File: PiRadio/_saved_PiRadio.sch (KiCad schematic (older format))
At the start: 2 parts

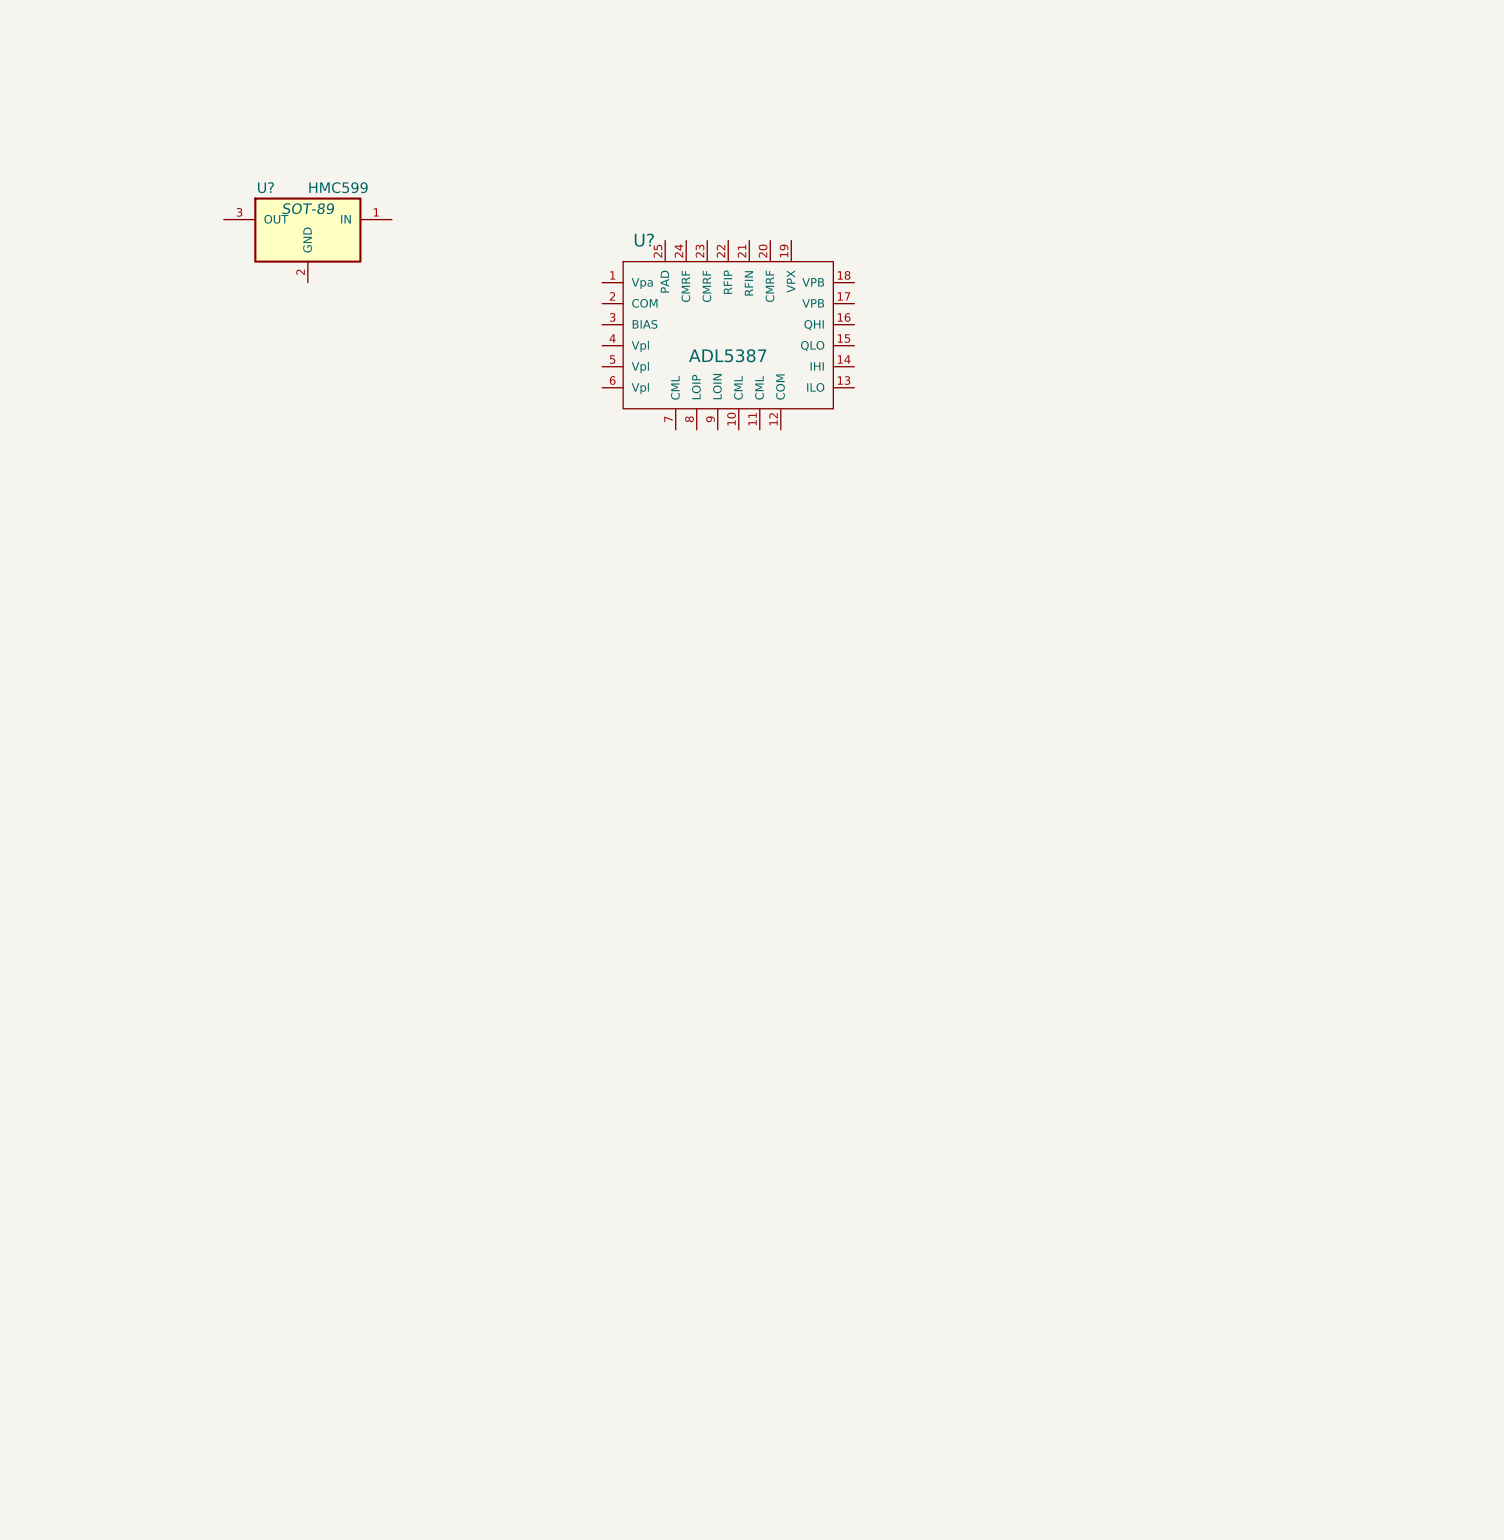
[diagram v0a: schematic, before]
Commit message: changes of CompLib and Shem
add IQ-Dec & PLL
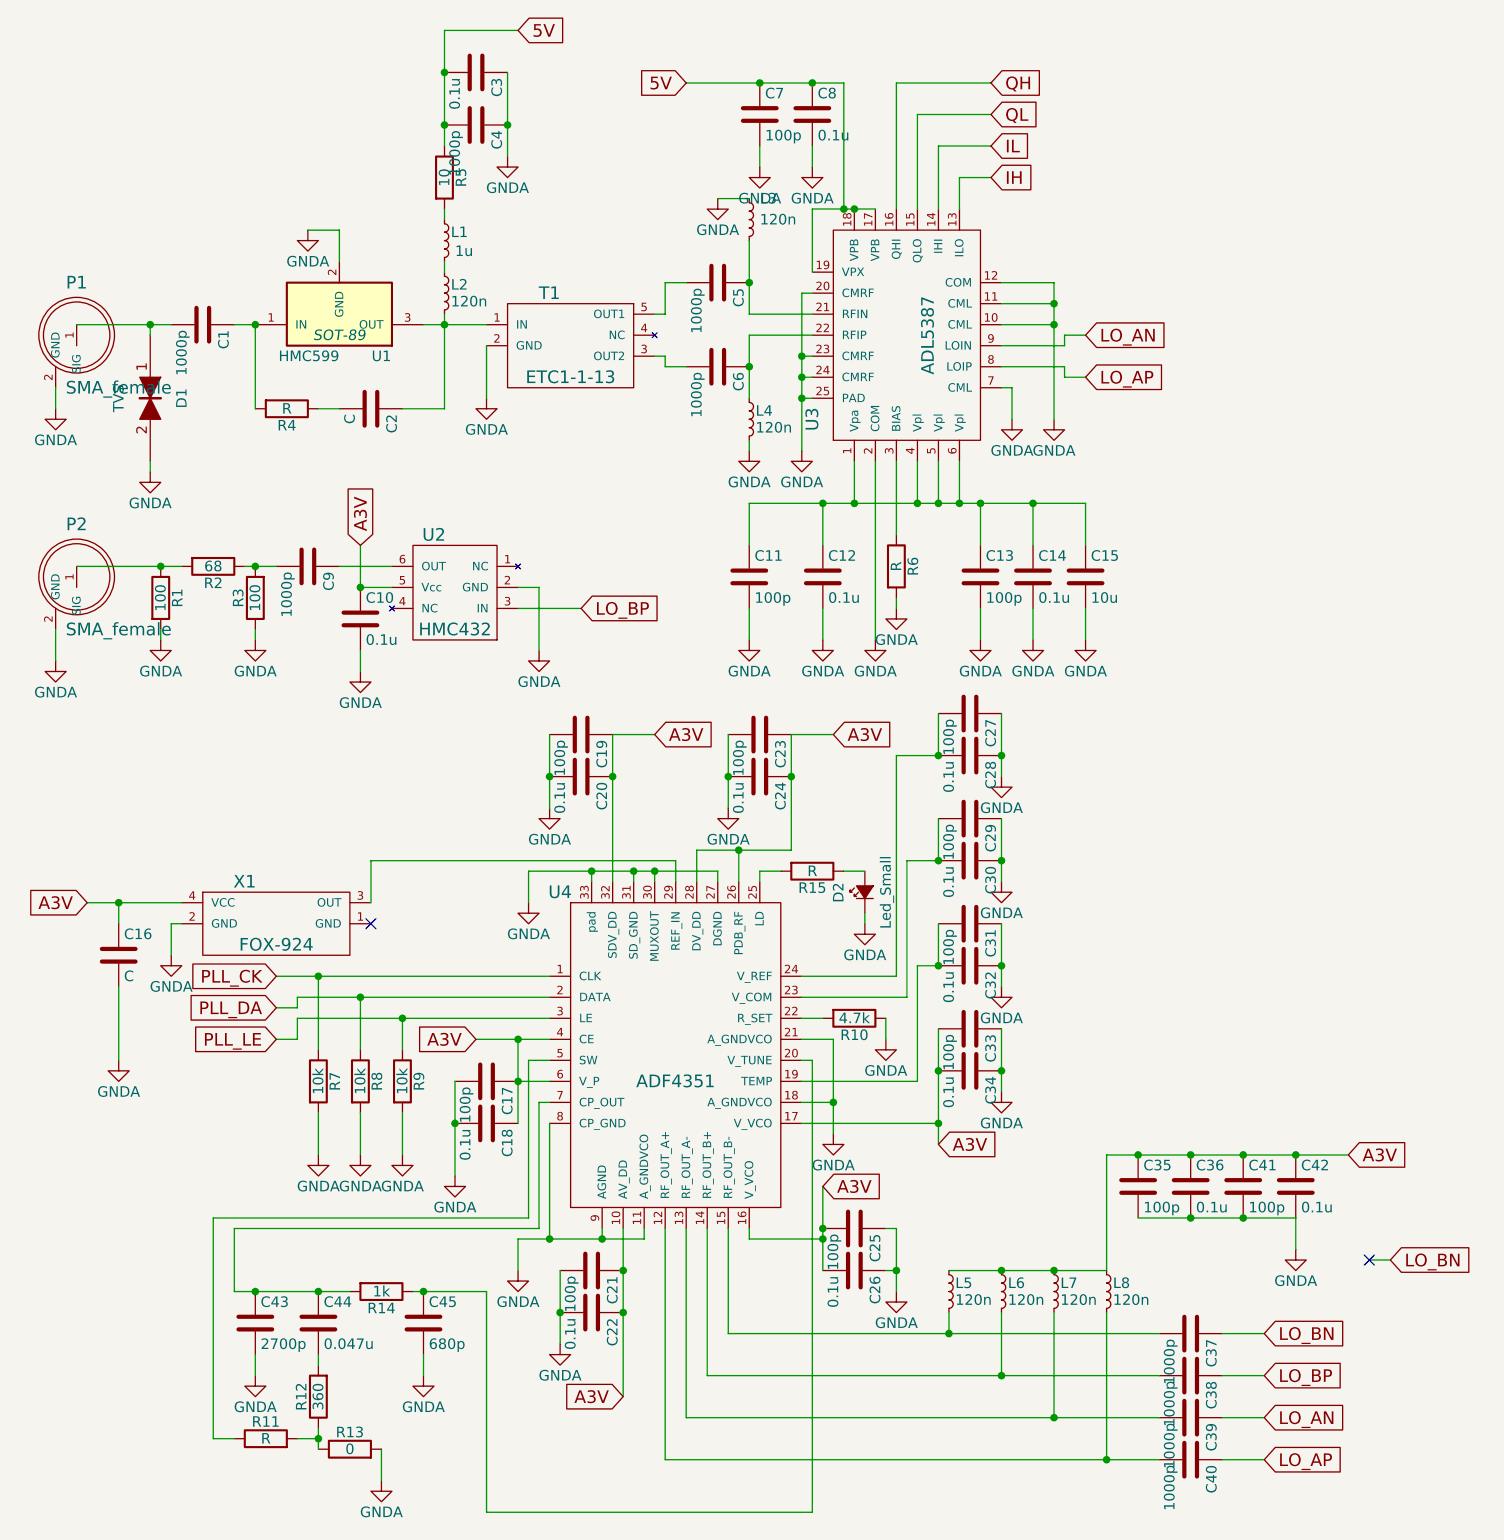
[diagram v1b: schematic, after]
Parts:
- added C1, C37, C38, C39, C4, C40, C5, C6, C9: 1000p, symbol C
- added C10, C12, C14, C18, C20, C22, C24, C26, C28, C3, C30, C32, C34, C36, C42, C8: 0.1u, symbol C
- added C11, C13, C17, C19, C21, C23, C25, C27, C29, C31, C33, C35, C41, C7: 100p, symbol C
- added C15: 10u, symbol C
- added C16, C2: C, symbol C
- added C43: 2700p, symbol C
- added C44: 0.047u, symbol C
- added C45: 680p, symbol C
- added D1: TVS, symbol TVS
- added D2: Led_Small, symbol Led_Small
- added L1: 1u, symbol L_Small
- added L2, L3, L4, L5, L6, L7, L8: 120n, symbol L_Small
- added P1, P2: SMA_female, symbol SMA_female
- added R1, R3: 100, symbol R
- added R10: 4.7k, symbol R
- added R11, R15, R4, R6: R, symbol R
- added R12: 360, symbol R
- added R13: 0, symbol R
- added R14: 1k, symbol R
- added R2: 68, symbol R
- added R5: 10, symbol R
- added R7, R8, R9: 10k, symbol R
- added T1: ETC1-1-13, symbol ETC1-1-13
- added U2: HMC432, symbol HMC432
- added U4: ADF4351, symbol ADF4351
- added X1: FOX-924, symbol FOX-924
- gave numbers to parts that had none: 2
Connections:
- net at U1.1 (IN): now also C1.1, R4.2
- net GNDA: now reaches U1.2 (GND)
- net GNDA: now also U3.10 (CML), U3.11 (CML), U3.12 (COM), U3.2 (COM), U3.20 (CMRF), U3.23 (CMRF), U3.24 (CMRF), U3.25 (PAD), U3.7 (CML), C10.2, C11.2, C12.2, C13.2, C14.2, C15.2, C16.2, C17.2, C18.2, C19.2, C20.2, C21.2, C22.2, C23.2, C24.2, C25.1, C26.1, C27.1, C28.1, C29.1, C3.1, C30.1, C31.1, C32.1, C33.1, C34.1, C35.2, C36.2, C4.1, C41.2, C42.2, C43.2, C45.2, C7.2, C8.2, D1.2, D2.1 (K), L3.1, L4.2, P1.2 (GND), P2.2 (GND), R1.2, R10.1, R13.2, R3.1, R6.2, R7.2, R8.2, R9.2, T1.2 (GND), U2.2 (GND), U4.11 (A_GNDVCO), U4.18 (A_GNDVCO), U4.21 (A_GNDVCO), U4.27 (DGND), U4.30 (MUXOUT), U4.31 (SD_GND), U4.33 (pad), U4.8 (CP_GND), U4.9 (AGND), X1.2 (GND)
- net at U1.3 (OUT): now also C2.1, L2.2, T1.1 (IN)
- net at U3.1 (Vpa): now also U3.4 (Vpl), U3.5 (Vpl), U3.6 (Vpl), C11.1, C12.1, C13.1, C14.1, C15.1
- net IH: now reaches U3.13 (ILO)
- net IL: now reaches U3.14 (IHI)
- net QL: now reaches U3.15 (QLO)
- net QH: now reaches U3.16 (QHI)
- net 5V: now reaches U3.17 (VPB)
- net 5V: now also U3.18 (VPB), U3.19 (VPX), C3.2, C4.2, C7.1, C8.1, R5.1
- net at U3.21 (RFIN): now also C5.1, L3.2
- net at U3.22 (RFIP): now also C6.1, L4.1
- net at U3.3 (BIAS): now also R6.1
- net LO_AP: now reaches U3.8 (LOIP)
- net LO_AP: now also C40.1
- net LO_AN: now reaches U3.9 (LOIN)
- net LO_AN: now also C39.1
- new net: C1.2, D1.1, P1.1 (SIG)
- new net: C2.2, R4.1
- new net: L1.1, R5.2
- new net: L1.2, L2.1
- new net: C6.2, T1.3 (OUT2)
- new net: C5.2, T1.5 (OUT1)
- new net: C9.1, U2.6 (OUT)
- new net: C9.2, R2.1, R3.2
- new net: P2.1 (SIG), R1.1, R2.2
- new net: C40.2, L8.2, U4.12 (RF_OUT_A+)
- new net: C39.2, L7.2, U4.13 (RF_OUT_A-)
- new net: C38.2, L6.2, U4.14 (RF_OUT_B+)
- new net: C37.2, L5.2, U4.15 (RF_OUT_B-)
- new net: C31.2, C32.2, U4.19 (TEMP)
- new net: C45.1, R14.1, U4.20 (V_TUNE)
- new net: R10.2, U4.22 (R_SET)
- new net: C29.2, C30.2, U4.23 (V_COM)
- new net: C27.2, C28.2, U4.24 (V_REF)
- new net: R15.2, U4.25 (LD)
- new net: U4.29 (REF_IN), X1.3 (OUT)
- new net: R11.1, U4.5 (SW)
- new net: C43.1, C44.1, R14.2, U4.7 (CP_OUT)
- new net: C44.2, R12.2
- new net: R11.2, R12.1, R13.1
- new net: D2.2 (A), R15.1
- new net A3V: C10.1, C16.1, C17.1, C18.1, C19.1, C20.1, C21.1, C22.1, C23.1, C24.1, C25.2, C26.2, C33.2, C34.2, C35.1, C36.1, C41.1, C42.1, L5.1, L6.1, L7.1, L8.1, U2.5 (Vcc), U4.10 (AV_DD), U4.16 (V_VCO), U4.17 (V_VCO), U4.26 (PDB_RF), U4.28 (DV_DD), U4.32 (SDV_DD), U4.4 (CE), U4.6 (V_P), X1.4 (VCC)
- new net LO_BN: C37.1
- new net LO_BP: C38.1, U2.3 (IN)
- new net PLL_CK: R7.1, U4.1 (CLK)
- new net PLL_DA: R8.1, U4.2 (DATA)
- new net PLL_LE: R9.1, U4.3 (LE)
- no-connect marks 0 -> 2
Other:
- moved on the sheet: U1, U3
